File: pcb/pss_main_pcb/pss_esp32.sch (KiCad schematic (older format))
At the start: 2 parts

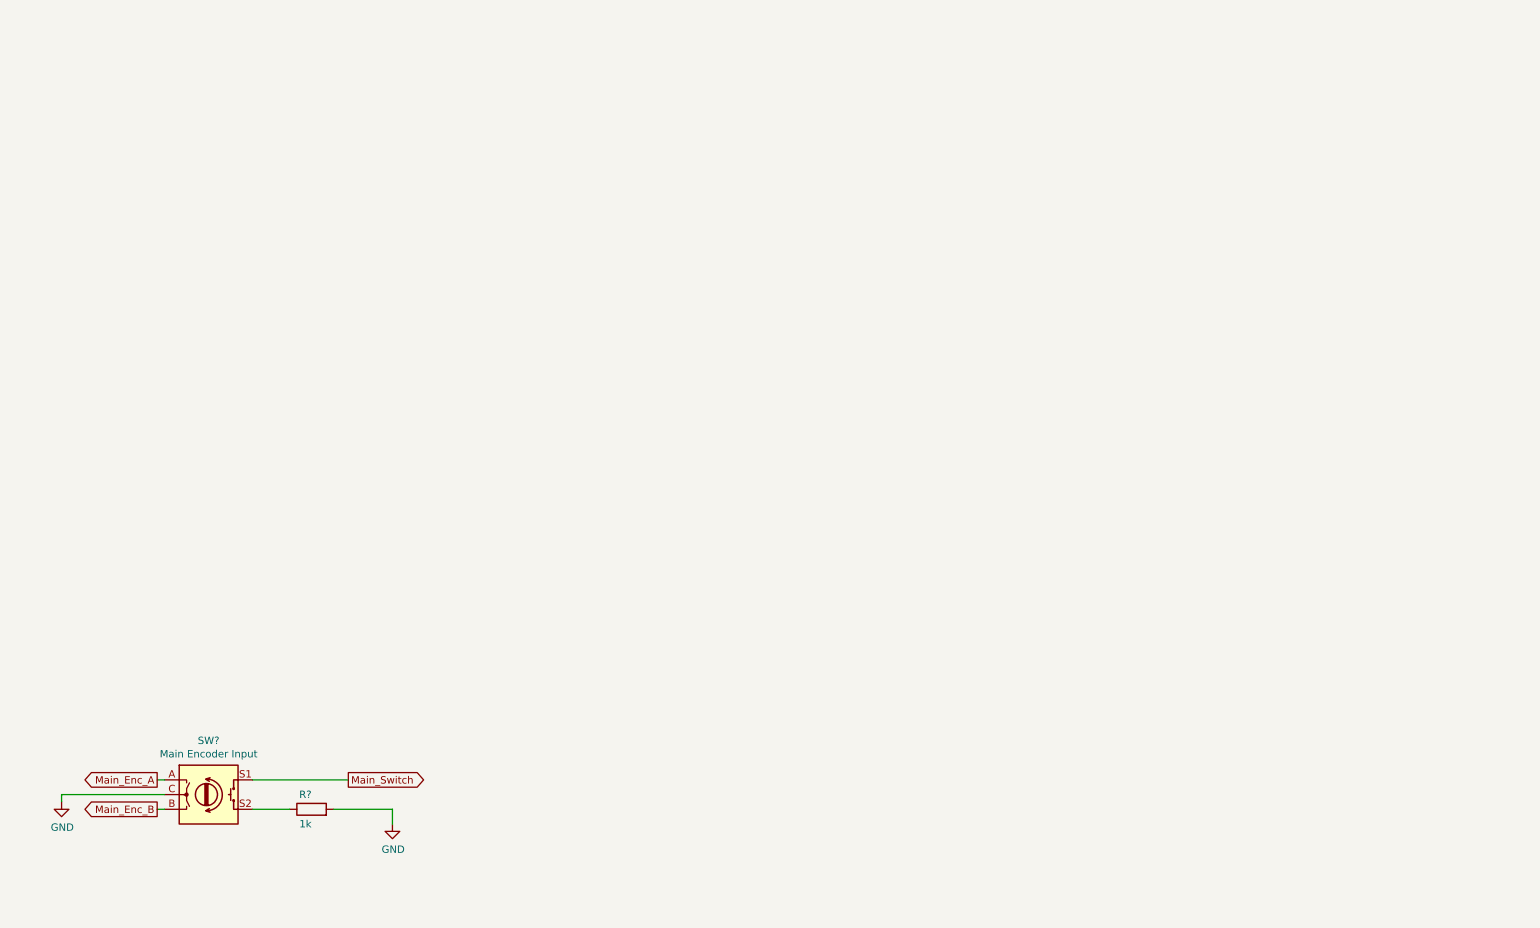
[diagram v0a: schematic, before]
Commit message: Add ESP32 list
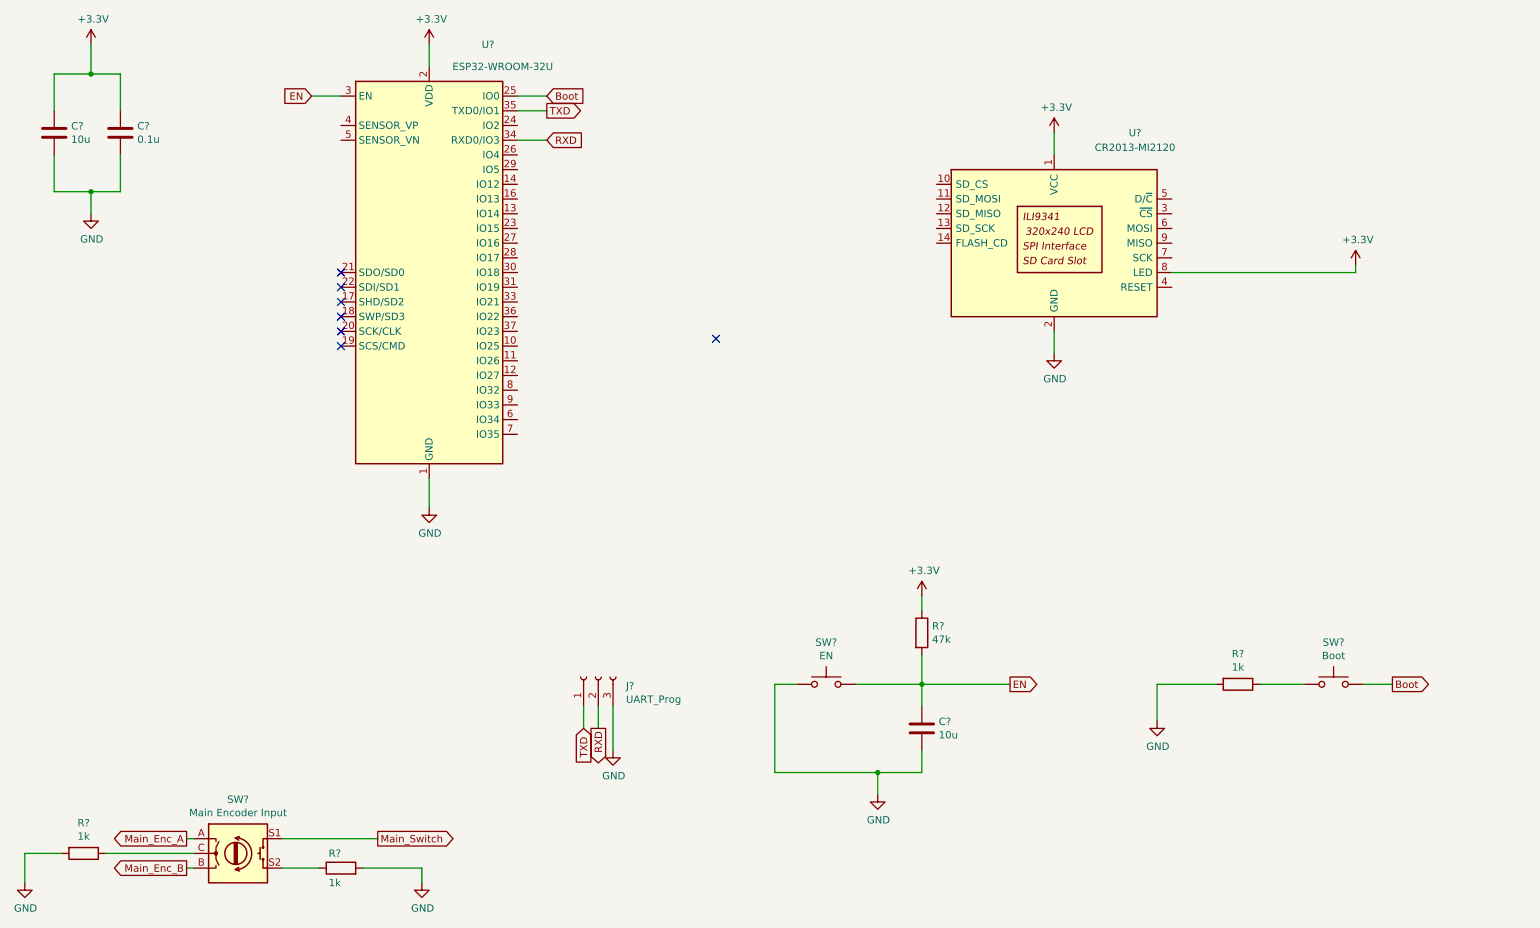
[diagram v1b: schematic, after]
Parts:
- added C? (x2): 10u, symbol Device:C
- added C?: 0.1u, symbol Device:C
- added J?: UART_Prog, symbol Connector:Conn_01x03_Female
- added R? (x2): 1k, symbol Device:R
- added R?: 47k, symbol Device:R
- added SW?: EN, symbol Switch:SW_Push
- added SW?: Boot, symbol Switch:SW_Push
- added U?: ESP32-WROOM-32U, RF_Module:ESP32-WROOM-32U, symbol RF_Module:ESP32-WROOM-32U
- added U?: CR2013-MI2120, Display:CR2013-MI2120, symbol Driver_Display:CR2013-MI2120
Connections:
- net GND: now also C?.2, C?.2, C?.2, J?.3 (Pin_3), R?.2, R?.2, SW?.1, U?.1 (GND), U?.15 (GND), U?.2 (GND), U?.38 (GND), U?.39 (GND); no longer SW?.C
- new net: R?.1, SW?.C
- new net: R?.1, SW?.1
- new net +3V3: C?.1, C?.1, R?.1, U?.1 (VCC), U?.2 (VDD), U?.8 (LED)
- new net Boot: SW?.2, U?.25 (IO0)
- new net EN: C?.1, R?.2, SW?.2, U?.3 (EN)
- new net RXD: J?.2 (Pin_2), U?.34 (RXD0/IO3)
- new net TXD: J?.1 (Pin_1), U?.35 (TXD0/IO1)
- no-connect marks 0 -> 7
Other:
- moved on the sheet: R?, SW?

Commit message: Add ESP32 to display and STM32 connections
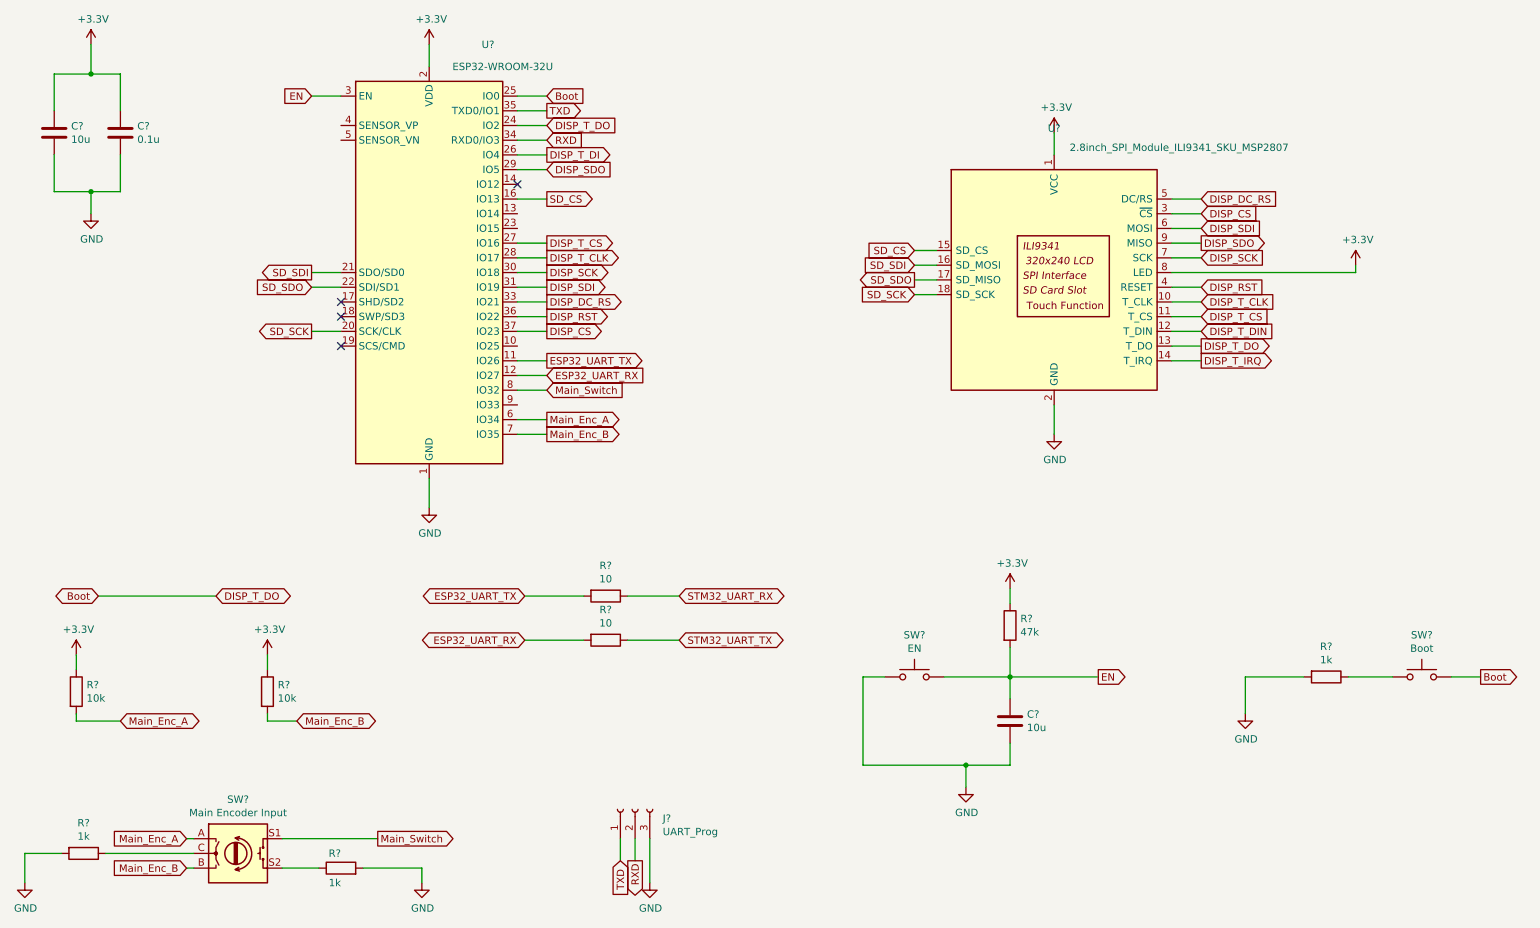
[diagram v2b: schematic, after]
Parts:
- removed U?: CR2013-MI2120, Display:CR2013-MI2120, symbol Driver_Display:CR2013-MI2120
- added R? (x2): 10k, symbol Device:R
- added R? (x2): 10, symbol Device:R
- added U?: 2.8inch_SPI_Module_ILI9341_SKU_MSP2807, Display:MSP2807, symbol display:2.8inch_SPI_Module_ILI9341_SKU_MSP2807
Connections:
- net +3V3: now also R?.1, R?.1, U?.1 (VCC), U?.8 (LED)
- net Boot: now also U?.24 (IO2), U?.13 (T_DO)
- net GND: now also U?.2 (GND)
- net Main_Enc_A: now also U?.6 (IO34), R?.2
- net Main_Enc_B: now also U?.7 (IO35), R?.2
- net Main_Switch: now also U?.8 (IO32)
- net ESP32_UART_TX: now reaches U?.11 (IO26)
- net ESP32_UART_TX: now also R?.2
- net ESP32_UART_RX: now reaches U?.12 (IO27)
- net ESP32_UART_RX: now also R?.2
- net SD_CS: now reaches U?.16 (IO13)
- net SD_CS: now also U?.15 (SD_CS)
- net SD_SCK: now reaches U?.20 (SCK/CLK)
- net SD_SCK: now also U?.18 (SD_SCK)
- net SD_SDI: now reaches U?.21 (SDO/SD0)
- net SD_SDI: now also U?.16 (SD_MOSI)
- net SD_SDO: now reaches U?.22 (SDI/SD1)
- net SD_SDO: now also U?.17 (SD_MISO)
- net DISP_T_DI: now reaches U?.26 (IO4)
- net DISP_T_CS: now reaches U?.27 (IO16)
- net DISP_T_CS: now also U?.11 (T_CS)
- net DISP_T_CLK: now reaches U?.28 (IO17)
- net DISP_T_CLK: now also U?.10 (T_CLK)
- net DISP_SDO: now reaches U?.29 (IO5)
- net DISP_SDO: now also U?.9 (MISO)
- net DISP_SCK: now reaches U?.30 (IO18)
- net DISP_SCK: now also U?.7 (SCK)
- net DISP_SDI: now reaches U?.31 (IO19)
- net DISP_SDI: now also U?.6 (MOSI)
- net DISP_DC_RS: now reaches U?.33 (IO21)
- net DISP_DC_RS: now also U?.5 (DC/RS)
- net DISP_RST: now reaches U?.36 (IO22)
- net DISP_RST: now also U?.4 (RESET)
- net DISP_CS: now reaches U?.37 (IO23)
- net DISP_CS: now also U?.3 (~CS)
- new net DISP_T_DIN: U?.12 (T_DIN)
- new net DISP_T_IRQ: U?.14 (T_IRQ)
- new net STM32_UART_RX: R?.1
- new net STM32_UART_TX: R?.1
- no-connect marks 7 -> 4
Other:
- moved on the sheet: C?, J?, R?, SW?

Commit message: Fix schematics
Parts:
- gave numbers to parts that had none: 17
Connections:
- net DISP_T_DI is gone; now on net DISP_T_DIN: U6.26 (IO4)
- net Boot: no longer U6.24 (IO2)
- net DISP_T_IRQ: now also U6.24 (IO2)
- net STM32_UART_RX renamed STM_UART_RX
- net STM32_UART_TX renamed STM_UART_TX
- no-connect marks 4 -> 10

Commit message: Add footprints
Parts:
- C20, C21, C22: footprint (none) -> Capacitor_SMD:C_1206_3216Metric_Pad1.42x1.75mm_HandSolder
- J6: footprint (none) -> Connector_PinHeader_2.54mm:PinHeader_1x03_P2.54mm_Vertical
- R31, R32, R33, R34, R35, R36, R37, R38: footprint (none) -> Resistor_SMD:R_1206_3216Metric_Pad1.42x1.75mm_HandSolder
- SW4: footprint (none) -> Rotary_Encoder:RotaryEncoder_Alps_EC11E-Switch_Vertical_H20mm
- SW5, SW6: footprint (none) -> Button_Switch_SMD:SW_SPST_B3S-1000
- U7: footprint Display:MSP2807 -> display:MSP2807
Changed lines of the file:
@@
 F 0 "SW4" H 2200 7017 50  0000 C CNN
 F 1 "Main Encoder Input" H 2200 6926 50  0000 C CNN
-F 2 "" H 2050 6810 50  0001 C CNN
+F 2 "Rotary_Encoder:RotaryEncoder_Alps_EC11E-Switch_Vertical_H20mm" H 2050 6810 50  0001 C CNN
 F 3 "~" H 2200 6910 50  0001 C CNN
 	1    2200 6650
@@
 F 0 "R34" V 3000 6750 50  0000 L CNN
 F 1 "1k" V 2800 6750 50  0000 L CNN
-F 2 "" V 2830 6750 50  0001 C CNN
+F 2 "Resistor_SMD:R_1206_3216Metric_Pad1.42x1.75mm_HandSolder" V 2830 6750 50  0001 C CNN
 F 3 "~" H 2900 6750 50  0001 C CNN
 	1    2900 6750
@@
 F 0 "R32" V 943 6650 50  0000 C CNN
 F 1 "1k" V 1034 6650 50  0000 C CNN
-F 2 "" V 1080 6650 50  0001 C CNN
+F 2 "Resistor_SMD:R_1206_3216Metric_Pad1.42x1.75mm_HandSolder" V 1080 6650 50  0001 C CNN
 F 3 "~" H 1150 6650 50  0001 C CNN
 	1    1150 6650
@@
 F 0 "C20" H 1065 1796 50  0000 L CNN
 F 1 "10u" H 1065 1705 50  0000 L CNN
-F 2 "" H 988 1600 50  0001 C CNN
+F 2 "Capacitor_SMD:C_1206_3216Metric_Pad1.42x1.75mm_HandSolder" H 988 1600 50  0001 C CNN
 F 3 "~" H 950 1750 50  0001 C CNN
 	1    950  1750
@@
 F 0 "C21" H 1515 1796 50  0000 L CNN
 F 1 "0.1u" H 1515 1705 50  0000 L CNN
-F 2 "" H 1438 1600 50  0001 C CNN
+F 2 "Capacitor_SMD:C_1206_3216Metric_Pad1.42x1.75mm_HandSolder" H 1438 1600 50  0001 C CNN
 F 3 "~" H 1400 1750 50  0001 C CNN
 	1    1400 1750
@@
 F 0 "J6" V 4838 6162 50  0000 R CNN
 F 1 "UART_Prog" V 4747 6162 50  0000 R CNN
-F 2 "" H 4900 6350 50  0001 C CNN
+F 2 "Connector_PinHeader_2.54mm:PinHeader_1x03_P2.54mm_Vertical" H 4900 6350 50  0001 C CNN
 F 3 "~" H 4900 6350 50  0001 C CNN
 	1    4900 6350
@@
 F 0 "SW5" H 6800 5735 50  0000 C CNN
 F 1 "EN" H 6800 5644 50  0000 C CNN
-F 2 "" H 6800 5650 50  0001 C CNN
+F 2 "Button_Switch_SMD:SW_SPST_B3S-1000" H 6800 5650 50  0001 C CNN
 F 3 "~" H 6800 5650 50  0001 C CNN
 	1    6800 5450
@@
 F 0 "SW6" H 10250 5735 50  0000 C CNN
 F 1 "Boot" H 10250 5644 50  0000 C CNN
-F 2 "" H 10250 5650 50  0001 C CNN
+F 2 "Button_Switch_SMD:SW_SPST_B3S-1000" H 10250 5650 50  0001 C CNN
 F 3 "~" H 10250 5650 50  0001 C CNN
 	1    10250 5450
@@
 F 0 "R38" V 9393 5450 50  0000 C CNN
 F 1 "1k" V 9484 5450 50  0000 C CNN
-F 2 "" V 9530 5450 50  0001 C CNN
+F 2 "Resistor_SMD:R_1206_3216Metric_Pad1.42x1.75mm_HandSolder" V 9530 5450 50  0001 C CNN
 F 3 "~" H 9600 5450 50  0001 C CNN
 	1    9600 5450
@@
 F 0 "R37" H 7520 5146 50  0000 L CNN
 F 1 "47k" H 7520 5055 50  0000 L CNN
-F 2 "" V 7380 5100 50  0001 C CNN
+F 2 "Resistor_SMD:R_1206_3216Metric_Pad1.42x1.75mm_HandSolder" V 7380 5100 50  0001 C CNN
 F 3 "~" H 7450 5100 50  0001 C CNN
 	1    7450 5100
@@
 F 0 "C22" H 7565 5796 50  0000 L CNN
 F 1 "10u" H 7565 5705 50  0000 L CNN
-F 2 "" H 7488 5600 50  0001 C CNN
+F 2 "Capacitor_SMD:C_1206_3216Metric_Pad1.42x1.75mm_HandSolder" H 7488 5600 50  0001 C CNN
 F 3 "~" H 7450 5750 50  0001 C CNN
 	1    7450 5750
@@
 F 0 "U7" H 7750 3281 50  0000 C CNN
 F 1 "2.8inch_SPI_Module_ILI9341_SKU_MSP2807" H 8600 3150 50  0000 C CNN
-F 2 "Display:MSP2807" H 7175 1375 50  0001 C CNN
+F 2 "display:MSP2807" H 7175 1375 50  0001 C CNN
 F 3 "http://pan.baidu.com/s/11Y990" H 7100 3000 50  0001 C CNN
 	1    7750 2500
@@
 F 0 "R31" H 1170 5596 50  0000 L CNN
 F 1 "10k" H 1170 5505 50  0000 L CNN
-F 2 "" V 1030 5550 50  0001 C CNN
+F 2 "Resistor_SMD:R_1206_3216Metric_Pad1.42x1.75mm_HandSolder" V 1030 5550 50  0001 C CNN
 F 3 "~" H 1100 5550 50  0001 C CNN
 	1    1100 5550
@@
 F 0 "R33" H 2470 5596 50  0000 L CNN
 F 1 "10k" H 2470 5505 50  0000 L CNN
-F 2 "" V 2330 5550 50  0001 C CNN
+F 2 "Resistor_SMD:R_1206_3216Metric_Pad1.42x1.75mm_HandSolder" V 2330 5550 50  0001 C CNN
 F 3 "~" H 2400 5550 50  0001 C CNN
 	1    2400 5550
@@
 F 0 "R35" V 4493 4900 50  0000 C CNN
 F 1 "10" V 4584 4900 50  0000 C CNN
-F 2 "" V 4630 4900 50  0001 C CNN
+F 2 "Resistor_SMD:R_1206_3216Metric_Pad1.42x1.75mm_HandSolder" V 4630 4900 50  0001 C CNN
 F 3 "~" H 4700 4900 50  0001 C CNN
 	1    4700 4900
@@
 F 0 "R36" V 4493 5200 50  0000 C CNN
 F 1 "10" V 4584 5200 50  0000 C CNN
-F 2 "" V 4630 5200 50  0001 C CNN
+F 2 "Resistor_SMD:R_1206_3216Metric_Pad1.42x1.75mm_HandSolder" V 4630 5200 50  0001 C CNN
 F 3 "~" H 4700 5200 50  0001 C CNN
 	1    4700 5200
